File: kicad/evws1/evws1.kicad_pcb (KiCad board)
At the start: 4 copper layers, 112 x 144 mm, 216 parts, among them J1 Screw_Terminal_01x03, J10 Screw_Terminal_01x04, J11 USB 2.0 Mini, J12 USB 2.0 Mini, J13 atmega-isp-6, J14 header, J15 Jumper, J16 header, J17 header, J18 header, J19 header, J2 Screw_Terminal_01x02, J20 header, J3 HB9500-2P, J4 HB9500-3P, J5 Screw_Terminal_01x04, J6 Screw_Terminal_01x03, J7 Screw_Terminal_01x02, J8 HB9500-2P, J9 HB9500-3P, K1 G3MB-202P, K2 G3MB-202P, M1 HLK-PM01, M2 dc-dc-buck-converter-5v-to-3.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, M3 dc-dc-converter-5v-to-p12v-m1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, M5 rpi-ev-plc-adapter-v1.0, Q1 AO3401, Q2 AO3401, Q3 AO3400, Q4 AO3400, Q5 AO3401, Q6 AO3401, Q7 AO3400, SW1 SW_SS13F06-G5, SW2 SW_SS13F06-G5, SW3 SW_Push, SW4 dip-switch-4x2pos-smd-1.27mm, SW5 SS-12D00G3, SW6 SS-12D00G3, SW7 SS-12D00G3, T1 ZMPT101B, T2 ZMPT101B, U1 atmega324p-20au, U10 max485esa, U11 PC817C, U12 LM258, U2 ACS712-30, U3 ACS712-30, U4 PCF8591, U5 ch340g, U6 ch340g, U7 DS1307ZN, U8 24LC512, U9 PCF8574, Y1 20MHz, Y2 12MHz, Y3 12MHz, Y4 32768kHz

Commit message: ...
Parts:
- added C40: 100n, Project:c-1206-hand-soldering, F.Cu at (249.4, -32.6)
- added C41: 10n, Project:c-1206-hand-soldering, F.Cu at (236.9, -34.9)
- added C42: 10n, Project:c-1206-hand-soldering, F.Cu at (236.9, -32.6)
- added C43: 10n, Project:c-1206-hand-soldering, F.Cu at (236.9, -30.4)
- added C44: 10n, Project:c-1206-hand-soldering, F.Cu at (243.2, -34.9)
- added C45: 1n, Project:c-1206-hand-soldering, F.Cu at (243.2, -32.6)
- added C46: 1n, Project:c-1206-hand-soldering, F.Cu at (249.4, -34.9)
- added C47: 1n, Project:c-1206-hand-soldering, F.Cu at (272.7, -40.5)
- added C48: 1n, Project:c-1206-hand-soldering, F.Cu at (279.0, -45.0)
- added C49: 1u, Project:c-1206-hand-soldering, F.Cu at (272.7, -42.8)
- added C50: 1u, Project:c-1206-hand-soldering, F.Cu at (272.7, -45.0)
- added C51: 100n, Project:c-1206-hand-soldering, F.Cu at (236.9, -23.6)
- added R76: 10R, Project:r-0805-hand-soldering, F.Cu at (263.5, 145.1)
- added R77: 10R, Project:r-0805-hand-soldering, F.Cu at (263.5, 146.9)
- added R78: 150R, Project:r-0805-hand-soldering, F.Cu at (268.0, 145.1)
- added R79: 330R, Project:r-0805-hand-soldering, F.Cu at (263.5, 148.8)
- added R80: 330R, Project:r-0805-hand-soldering, F.Cu at (268.0, 146.9)
- added R81: 820R, Project:r-0805-hand-soldering, F.Cu at (242.3, -28.7)
- added R82: 820R, Project:r-0805-hand-soldering, F.Cu at (246.7, -30.6)
- added R83: 1K2, Project:r-0805-hand-soldering, F.Cu at (254.8, -35.1)
- added R84: 1K2, Project:r-0805-hand-soldering, F.Cu at (259.2, -33.2)
- added R85: 18K, Project:r-0805-hand-soldering, F.Cu at (242.3, -30.6)
- added R86: 0R, Project:r-0805-hand-soldering, F.Cu at (246.7, -28.7)
- added R87: 18K, Project:r-0805-hand-soldering, F.Cu at (259.2, -35.1)
- added R88: 0R, Project:r-0805-hand-soldering, F.Cu at (251.2, -30.6)
- added R89: 15K, Project:r-0805-hand-soldering, F.Cu at (251.2, -28.7)
- added R90: 15K, Project:r-0805-hand-soldering, F.Cu at (254.8, -33.2)
- added R91: 22K, Project:r-0805-hand-soldering, F.Cu at (278.1, -43.0)
- added R92: 22K, Project:r-0805-hand-soldering, F.Cu at (278.1, -41.1)
- added R93: 560R, Project:r-0805-hand-soldering, F.Cu at (278.1, -39.3)
- added RV2: 100R, Project:trimmer-tht-3296, F.Cu at (262.7, -38.5)
- added RV3: 100R, Project:trimmer-tht-3296, F.Cu at (257.4, -38.5)
- added RV4: 1K, Project:trimmer-tht-3296, F.Cu at (252.2, -38.5)
- added RV5: 1K, Project:trimmer-tht-3296, F.Cu at (246.9, -38.5)
- added RV6: 1K, Project:trimmer-tht-3296, F.Cu at (241.7, -38.5)
- added RV7: 1K, Project:trimmer-tht-3296, F.Cu at (236.4, -38.5)
- added U13: LM224, Project:soic-16_hand-soldering, F.Cu at (288.3, -12.9)
- R18: value 22K -> 10K
- R59, R60: value 22k -> 100R
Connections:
- net VREF-2V5 renamed /Measurement/VREF+2V5
- C27 pad 2: +3V3 -> +12V
- C28 pad 1: /Microcontroller/AD-VC2 -> Net-(C28-Pad1)
- D11 pad 1: /Microcontroller/AD-VC2 -> Net-(C28-Pad1)
- D16 pad 1: (no net) -> /MODBUS-B
- D16 pad 2: (no net) -> /MODBUS-A
- D16 pad 3: (no net) -> GND
- D9 pad 3: Net-(D9-Pad3) -> (no net)
- J17 pad 1: (no net) -> GND
- J17 pad 2: (no net) -> Net-(J17-Pad2)
- J17 pad 3: (no net) -> Net-(J17-Pad3)
- J18 pad 1: (no net) -> /MODBUS-A
- J18 pad 2: (no net) -> Net-(J18-Pad2)
- J19 pad 1: (no net) -> /MODBUS-B
- J19 pad 2: (no net) -> Net-(J19-Pad2)
- J20 pad 1: (no net) -> Net-(J20-Pad1)
- J20 pad 2: (no net) -> /MODBUS-A
- J6 pad 1: (no net) -> /MODBUS-A
- J6 pad 2: (no net) -> /MODBUS-B
- R53 pad 2: Net-(D9-Pad3) -> Net-(R53-Pad2)
- R54 pad 1: Net-(D9-Pad3) -> Net-(R53-Pad2)
- R59 pad 1: Net-(R59-Pad1) -> Net-(C41-Pad1)
- R59 pad 2: GND -> /Measurement/V1P
- R6 pad 1: V1P -> /Measurement/V1P
- R6 pad 2: V1N -> GND
- R60 pad 1: Net-(R60-Pad1) -> Net-(C42-Pad1)
- R60 pad 2: GND -> /Measurement/V2P
- R61 pad 1: /Microcontroller/AD-VC2 -> Net-(C28-Pad1)
- R7 pad 1: V2P -> /Measurement/V2P
- R7 pad 2: V2N -> GND
- T1 pad 3: V1P -> /Measurement/V1P
- T1 pad 4: V1N -> GND
- T2 pad 3: V2N -> GND
- T2 pad 4: V2P -> /Measurement/V2P
- U1 pad 34: (no net) -> /Measurement/AD-I2
- U1 pad 35: (no net) -> /Measurement/AD-V2
- U1 pad 36: (no net) -> /Measurement/AD-I1
- U1 pad 37: (no net) -> /Measurement/AD-V1
- U10 pad 6: (no net) -> Net-(J17-Pad2)
- U10 pad 7: (no net) -> Net-(J17-Pad3)
- U12 pad 2: /Microcontroller/AD-VC2 -> Net-(C28-Pad1)
- U12 pad 3: Net-(D9-Pad3) -> Net-(R53-Pad2)
- U12 pad 4: GND -> -12V
- U12 pad 5: Net-(R59-Pad1) -> GND
- U12 pad 6: Net-(R60-Pad1) -> Net-(R91-Pad1)
- U12 pad 7: (no net) -> /Measurement/VREF-2V5
- U12 pad 8: +3V3 -> +12V
- U2 pad 7: (no net) -> /Measurement/I1
- U3 pad 7: (no net) -> /Measurement/I2

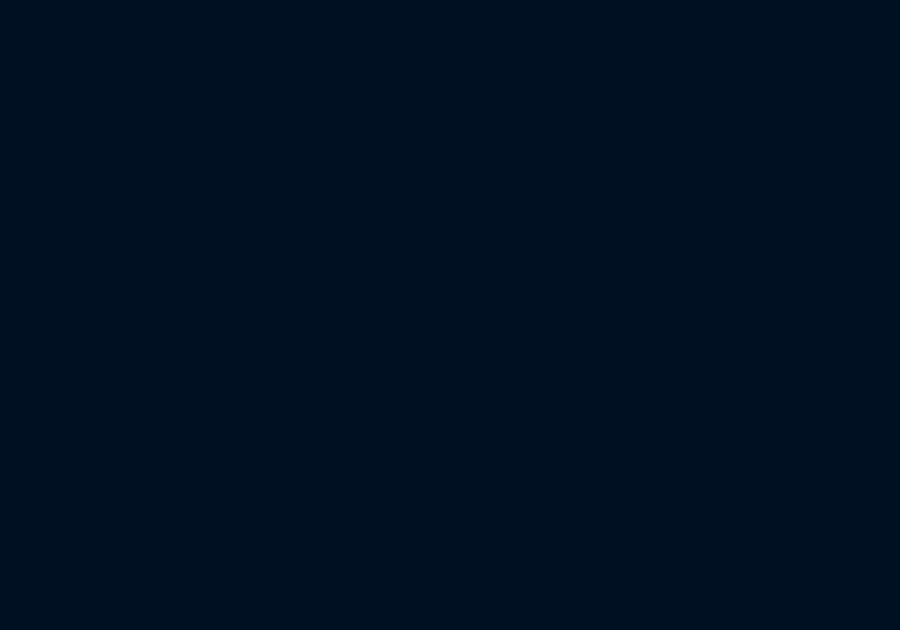
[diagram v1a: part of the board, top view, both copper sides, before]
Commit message: Schematic completed, no DRC errors left
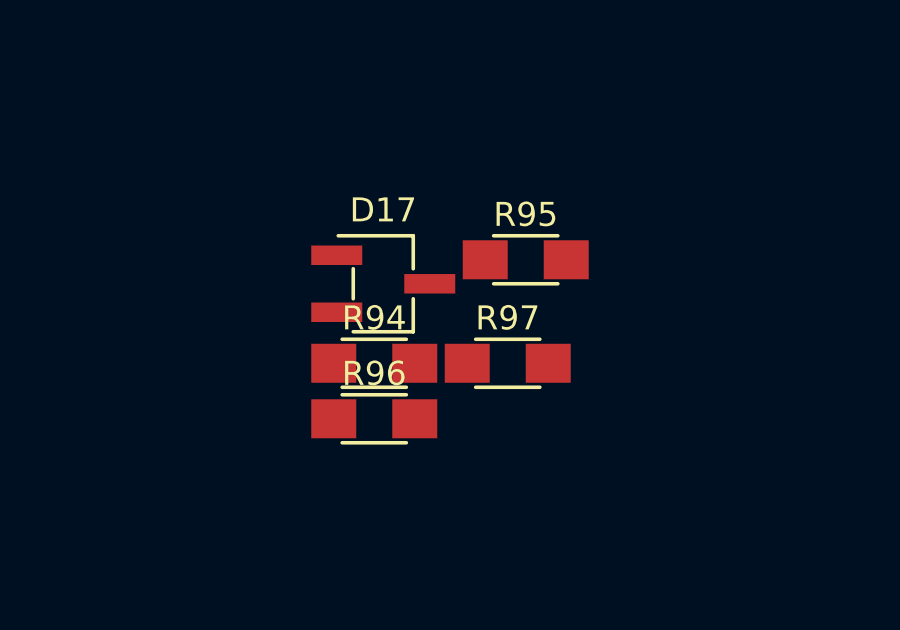
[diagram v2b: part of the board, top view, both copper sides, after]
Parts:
- added D17: BAT54S, Project:sot-23_hand-soldering, F.Cu at (196.8, -15.3)
- added R94: 100R, Project:r-0805-hand-soldering, F.Cu at (196.5, -12.7)
- added R95: 100R, Project:r-0805-hand-soldering, F.Cu at (201.6, -16.1)
- added R96: 47K, Project:r-0805-hand-soldering, F.Cu at (196.5, -10.8)
- added R97: 47K, Project:r-0805-hand-soldering, F.Cu at (201.0, -12.7)
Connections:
- net Net-(J5-Pad1) renamed /EV1TP
- D9 pad 2: +3V3 -> +5V
- D9 pad 3: (no net) -> /EV1X
- J10 pad 1: Net-(J10-Pad1) -> /EV2TP
- J10 pad 3: (no net) -> GND
- JP1 pad 2: Net-(J10-Pad1) -> (no net)
- R76 pad 1: (no net) -> /MODBUS-A
- SW4 pad 5: (no net) -> /EV1X
- SW4 pad 7: (no net) -> /EV2X
- TP1 pad 1: Net-(J10-Pad1) -> /EV2TP
- U9 pad 4: (no net) -> /Microcontroller/K2-IS-ON
- U9 pad 5: /Microcontroller/K2-IS-ON -> /Microcontroller/K1-IS-ON
- U9 pad 6: /Microcontroller/K1-IS-ON -> /EV1X
- U9 pad 7: (no net) -> /EV2X

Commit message: schematic finished
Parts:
- added D18: BAT54S, Project:sot-23_hand-soldering, F.Cu at (402.9, 27.9)
- added D19: BAT54S, Project:sot-23_hand-soldering, F.Cu at (402.9, 31.4)
- added D20: LED, LEDs:LED_0805_HandSoldering, F.Cu at (129.4, -16.4)
- added J21: header, Project:idc-header-1x03-p2.54mm-vertical, F.Cu at (395.9, 27.7)
- added J22: header, Project:idc-header-1x03-p2.54mm-vertical, F.Cu at (398.9, 27.7)
- added J23: header, Project:idc-header-1x02-p2.54mm-vertical, F.Cu at (128.5, -21.4)
- added J24: header, Project:idc-header-1x03-p2.54mm-vertical, F.Cu at (320.7, 48.1)
- added J25: header, Project:idc-header-1x04-p2.54mm-vertical, F.Cu at (167.1, 88.2)
- added R100: 47K, Project:r-0805-hand-soldering, F.Cu at (132.2, -20.2)
- added R101: 47K, Project:r-0805-hand-soldering, F.Cu at (132.2, -18.3)
- added R102: 220R, Project:r-0805-hand-soldering, F.Cu at (134.0, -16.5)
- added R103: 1K, Project:r-0805-hand-soldering, F.Cu at (136.7, -20.2)
- added R104: 270R, Project:r-0805-hand-soldering, F.Cu at (321.5, 55.6)
- added R105: 560R, Project:r-0805-hand-soldering, F.Cu at (324.4, 47.5)
- added R98: 47K, Project:r-0805-hand-soldering, F.Cu at (132.2, -22.0)
- added R99: 47K, Project:r-0805-hand-soldering, F.Cu at (136.7, -22.0)
- added SW8: dip-switch-4x2pos-smd-1.27mm, Project:dip-switch-4x2pos-smd-1.27mm, F.Cu at (315.6, 51.5)
- added TP7: TestPoint, Measurement_Points:Measurement_Point_Round-TH_Small, F.Cu at (115.2, 59.7)
- added TP8: TestPoint, Wire_Pads:SolderWirePad_single_0-8mmDrill, F.Cu at (79.8, 22.4)
- added TP9: TestPoint, Wire_Pads:SolderWirePad_single_0-8mmDrill, F.Cu at (165.8, 43.7)
- C23: footprint Capacitors_THT:C_Disc_D3.8mm_W2.6mm_P2.50mm -> Project:capacitor-ceramic-tht-2200pf-1000v
- R1: value 220K -> 0R; footprint Project:r-0805-hand-soldering -> Project:r-1206-hand-soldering
- R27, R28: value 1K -> 10K
- R6, R7: value 100R -> 1K
- R62, R72: value 100R -> 180R
- R83, R84: value 1K2 -> 3K3
- R85, R87: value 18K -> 15K
- R86, R88: value 0R -> 4K7
- R89, R90: value 15K -> 10K
- R94, R95: value 100R -> 330R
- TP1, TP4: footprint Measurement_Points:Measurement_Point_Round-TH_Big -> Measurement_Points:Measurement_Point_Round-TH_Small
- moved C23 8.82 mm to (266.2, 26.3)
- moved C1 1.98 mm to (53.2, 98.4)
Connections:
- C43 pad 2: /Measurement/AD-V1 -> Net-(C43-Pad2)
- C44 pad 2: /Measurement/AD-V2 -> Net-(C44-Pad2)
- D7 pad 3: /Microcontroller/MISO -> /Microcontroller/Converter-And-Cp/MISO-IN
- D8 pad 3: /Microcontroller/IRQ-MODEM -> /Microcontroller/Converter-And-Cp/IRQ-IN
- JP2 pad 1: /Microcontroller/CONNECTED -> Net-(JP2-Pad1)
- JP3 pad 1: /Microcontroller/CONNECTED -> Net-(JP2-Pad1)
- R6 pad 1: /Measurement/V1P -> /Measurement/AD-V1
- R6 pad 2: GND -> Net-(C43-Pad2)
- R7 pad 1: /Measurement/V2P -> /Measurement/AD-V2
- R7 pad 2: GND -> Net-(C44-Pad2)
- R89 pad 1: /Measurement/AD-V1 -> Net-(C43-Pad2)
- R90 pad 1: /Measurement/AD-V2 -> Net-(C44-Pad2)
- SW5 pad 1: Net-(Q3-Pad1) -> Net-(R22-Pad2)
- SW5 pad 2: Net-(R22-Pad2) -> Net-(Q3-Pad1)
- SW5 pad 3: (no net) -> Net-(R102-Pad2)
- T1 pad 2: /N-K1 -> /N-EV1
- T1 pad 3: /Measurement/V1P -> GND
- T1 pad 4: GND -> /Measurement/V1P
- U1 pad 21: /Microcontroller/IRQ-MODEM -> /Microcontroller/IRQ-PORTEXP
- U1 pad 30: /Microcontroller/CONNECTED -> /Microcontroller/DEBUG
- U1 pad 31: /Microcontroller/IRQ-PORTEXP -> /Microcontroller/LCD-RW
- U1 pad 40: /Microcontroller/LCD-RS -> Net-(J24-Pad2)
- U1 pad 41: /Microcontroller/LCD-RW -> Net-(J24-Pad3)
- U1 pad 42: /Microcontroller/~K1-ON -> /Microcontroller/LCD-RS
- U1 pad 43: /Microcontroller/~K2-ON -> /Microcontroller/IRQ-MODEM
- U13 pad 14: /Measurement/AD-V2 -> Net-(C44-Pad2)
- U13 pad 7: /Measurement/AD-V1 -> Net-(C43-Pad2)
- U9 pad 10: (no net) -> /EV2X
- U9 pad 4: /Microcontroller/K2-IS-ON -> /Microcontroller/PEXP-P0
- U9 pad 5: /Microcontroller/K1-IS-ON -> /Microcontroller/PEXP-P1
- U9 pad 6: /EV1X -> /Microcontroller/K2-IS-ON
- U9 pad 7: /EV2X -> /Microcontroller/K1-IS-ON
- U9 pad 9: (no net) -> /EV1X

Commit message: ...
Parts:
- removed JP1: SolderJumper_3_Open, Pin_Headers:Pin_Header_Straight_1x03_Pitch2.54mm
- added C52: 100n, Project:c-1206-hand-soldering, B.Cu at (64.6, 103.5)
- added C53: 100n, Project:c-1206-hand-soldering, B.Cu at (117.9, 110.5)
- added C54: 100n, Project:c-1206-hand-soldering, B.Cu at (67.0, 111.3)
- added J26: header, Project:idc-header-1x02-p2.54mm-vertical, F.Cu at (92.7, 42.6)
- added U14: LM258, Project:soic-8_hand-soldering, B.Cu at (65.8, 107.4)
- BT1: footprint Project:knob-battery-holder-horizontal-tht -> Project:knob-battery-holder-vertical-tht
- C10, C11, C12, C13, C14, C15, C16, C17, C19, C20, C21, C22, C24, C25, C26, C27, C28, C37, C39, C40, C41, C42, C43, C44, C45, C46, C47, C48, C49, C50, C51, C6, C7, C8, C9, D1, D10, D11, D12, D13, D14, D15, D16, D17, D18, D19, D2, D5, D6, D7, D8, D9, L1, Q3, Q4, Q5, Q6, Q7, R1, R100, R101, R102, R103, R104, R105, R18, R19, R20, R21, R22, R23, R24, R25, R26, R27, R28, R29, R30, R31, R32, R33, R34, R35, R36, R37, R38, R39, R40, R41, R42, R43, R44, R45, R46, R47, R48, R49, R50, R51, R52, R53, R54, R55, R56, R57, R58, R59, R60, R61, R62, R63, R64, R65, R66, R67, R68, R69, R70, R71, R72, R73, R74, R75, R76, R77, R78, R79, R80, R81, R82, R83, R84, R85, R86, R87, R88, R89, R90, R91, R92, R93, R94, R95, R96, R97, R98, R99, U10, U11, U12, U4, U8, U9: moved to B.Cu
- C23: footprint Project:capacitor-ceramic-tht-2200pf-1000v -> Project:c-1206-hand-soldering; moved to B.Cu
- RV3: value 100R -> 1K
- RV4: value 1K -> 100R
- SW3: footprint Buttons_Switches_SMD:SW_SPST_FSMSM -> Project:push-button-smd-4.5x4.5mm-black
- U13: value LM224 -> LM258; footprint Project:soic-16_hand-soldering -> Project:soic-8_hand-soldering; moved to B.Cu
- U5, Y2: moved to F.Cu
- moved J22 349.7 mm to (58.8, 109.0), turned to 180 degrees
- moved D19 339.2 mm to (71.2, 102.4)
- moved D18 289.2 mm to (125.8, 111.0), turned to 90 degrees
- moved J21 278.9 mm to (129.3, 109.7), turned to 180 degrees
- moved J24 269.9 mm to (67.2, 140.6), turned to 90 degrees
- moved R105 266.1 mm to (62.1, 92.2), turned to 90 degrees
- moved R104 264.0 mm to (60.0, 92.0), turned to 270 degrees
- moved R87 250.5 mm to (64.0, 121.8)
- moved D9 243.5 mm to (27.2, 90.0)
- moved R88 240.0 mm to (64.0, 119.7), turned to 180 degrees
- moved RV4 238.9 mm to (77.2, 124.2)
- moved C46 238.6 mm to (68.3, 120.5), turned to 270 degrees
- moved RV7 232.1 mm to (70.9, 124.2)
- moved R84 231.7 mm to (76.9, 109.8)
- moved RV5 231.3 mm to (82.5, 124.2)
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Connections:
- net Net-(F1-Pad2) renamed /Microcontroller/UARTs/Modbus/UART0-5V
- net Net-(F2-Pad2) renamed /Microcontroller/UARTs/Modbus/UART1-5V
- net Net-(J11-Pad2) renamed /Microcontroller/UARTs/Modbus/USB0-D-
- net Net-(J11-Pad3) renamed /Microcontroller/UARTs/Modbus/USB0-D+
- net Net-(J12-Pad2) renamed /Microcontroller/UARTs/Modbus/USB1-D-
- net Net-(J12-Pad3) renamed /Microcontroller/UARTs/Modbus/USB1-D+
- D16 pad 1: /MODBUS-B -> /MODBUS-A
- D16 pad 2: /MODBUS-A -> /MODBUS-B
- J5 pad 1: /EV1TP -> /CP1
- J5 pad 2: /~EV1ON -> GND
- J5 pad 3: GND -> /~EV1ON
- J5 pad 4: /CP1 -> /EV1TP
- J6 pad 1: /MODBUS-A -> GND
- J6 pad 3: GND -> /MODBUS-A
- M1 pad 3: 230V-N -> 230V-L
- M1 pad 4: 230V-L -> 230V-N
- Q5 pad 2: +3V3 -> +5V
- R47 pad 2: +3V3 -> +5V
- R76 pad 2: Net-(J17-Pad2) -> Net-(J17-Pad3)
- R77 pad 2: Net-(J17-Pad3) -> Net-(J17-Pad2)
- RV3 pad 1: Net-(C42-Pad2) -> Net-(R85-Pad2)
- RV3 pad 2: Net-(C42-Pad2) -> Net-(R85-Pad2)
- RV3 pad 3: Net-(R82-Pad1) -> /Measurement/VREF-2V5
- RV4 pad 1: Net-(R85-Pad2) -> Net-(C42-Pad2)
- RV4 pad 2: Net-(R85-Pad2) -> Net-(C42-Pad2)
- RV4 pad 3: /Measurement/VREF-2V5 -> Net-(R82-Pad1)
- TP7 pad 1: +BATT -> /Microcontroller/AOUT
- U10 pad 6: Net-(J17-Pad2) -> Net-(J17-Pad3)
- U10 pad 7: Net-(J17-Pad3) -> Net-(J17-Pad2)
- U13 pad 8: Net-(C42-Pad2) -> -12V
- U4 pad 15: (no net) -> /Microcontroller/AOUT

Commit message: ...
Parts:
- M1: footprint Project:HLK-PM01 -> Project:HLK-PM01-5M05
- R10, R100, R101, R102, R103, R104, R105, R11, R12, R13, R14, R15, R16, R17, R18, R19, R2, R20, R21, R22, R23, R24, R25, R26, R27, R28, R29, R3, R30, R31, R32, R33, R34, R35, R36, R37, R38, R39, R4, R40, R42, R43, R44, R45, R46, R47, R48, R49, R5, R50, R51, R52, R53, R54, R55, R56, R57, R58, R59, R6, R60, R61, R62, R63, R64, R65, R66, R67, R68, R69, R7, R70, R71, R72, R73, R74, R75, R76, R77, R78, R79, R8, R80, R81, R82, R83, R84, R85, R86, R87, R88, R89, R9, R90, R91, R92, R93, R94, R95, R96, R97, R98, R99: footprint Project:r-0805-hand-soldering -> Project:r-1206-hand-soldering
- moved C47 144.9 mm to (8.05, 87.3)
- moved C48 144.9 mm to (14.8, 107.8)
- moved C49 144.9 mm to (7.85, 107.8)
- moved C50 144.9 mm to (1.25, 87.4)
- moved Q4 144.9 mm to (15.4, 91.2)
- moved Q5 144.9 mm to (14.9, 104.1)
- moved Q6 144.9 mm to (14.3, 84.2)
- moved Q7 144.9 mm to (22.2, 108.2)
- moved R46 144.9 mm to (14.1, 87.3)
- moved R47 144.9 mm to (19.7, 103.7)
- moved R48 144.9 mm to (9.75, 104.3)
- moved R49 144.9 mm to (8.15, 85.0)
- moved R50 144.9 mm to (18.6, 112.0)
- moved R51 144.9 mm to (20.4, 84.1)
- moved R52 144.9 mm to (27.6, 108.2)
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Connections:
- J18 pad 1: /MODBUS-A -> Net-(J18-Pad1)
- J18 pad 2: Net-(J18-Pad2) -> /MODBUS-A
- R78 pad 1: Net-(J18-Pad2) -> Net-(J18-Pad1)

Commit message: ...
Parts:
- removed C27: 100n, Project:c-1206-hand-soldering
- removed the R90 at (75.3, 106.5)
- removed the R93 at (199.8, 76.2)
- removed the TP2 at (101.5, 129.6)
- removed U14: LM258, Project:soic-8_hand-soldering
- added R106: 0R, Project:r-1206-hand-soldering, B.Cu at (124.4, 82.8)
- added R4: 10K, Project:r-1206-hand-soldering, F.Cu at (98.8, 114.7)
- added R5: 560R, Project:r-1206-hand-soldering, F.Cu at (92.7, 113.9)
- C10, C11, C12, C13, C16, C17, C28, C41, C42, C43, C44, C45, C46, C47, C48, C49, C50, C51, C6, C7, C8, C9, D11, D18, D19, D2, D5, L1, Q4, Q5, Q6, Q7, R18, R19, R46, R47, R48, R49, R50, R51, R52, R53, R54, R6, R61, R7, R81, R82, R83, R84, R85, R86, R87, R88, R89, R91, R92, U12: moved to F.Cu
- J21, J22: footprint Project:idc-header-1x03-p2.54mm-vertical -> Project:idc-header-1x04-p2.54mm-vertical
- M2, M3: moved to B.Cu
- TP3: footprint Wire_Pads:SolderWirePad_single_0-8mmDrill -> Measurement_Points:Measurement_Point_Round-TH_Small
- U13: value LM258 -> LM224; footprint Project:soic-8_hand-soldering -> Project:soic-14_hand-soldering; moved to F.Cu
- moved R33 298.5 mm to (-9.33, 132.1)
- moved R34 292.9 mm to (-2.65, 132.1)
- moved R32 263.3 mm to (14.2, 79.0), turned to 0 degrees
- moved U9 252.2 mm to (17.7, 87.7), turned to 90 degrees
- moved C22 247.1 mm to (24.4, 84.6), turned to 90 degrees
- moved R31 244.5 mm to (17.3, 97.2), turned to 180 degrees
- moved R24 240.8 mm to (27.6, 148.6)
- moved R39 240.8 mm to (32.1, 159.9)
- moved R25 240.8 mm to (27.4, 154.7)
- moved R35 240.8 mm to (27.3, 159.9)
- moved R36 240.8 mm to (27.2, 165.3)
- moved R40 240.8 mm to (31.9, 165.3)
- moved R37 240.8 mm to (32.9, 148.5)
- moved R38 240.8 mm to (32.4, 154.7)
- moved R18 144.4 mm to (78.0, 123.5), turned to 180 degrees
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- renumbered R4 to R90, R5 to R93, TP4 to TP2
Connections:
- C45 pad 2: /Measurement/AD-I1 -> /AD-I1
- C46 pad 2: /Measurement/AD-I2 -> /AD-I2
- D10 pad 2: /CP2 -> /CP1
- D18 pad 3: /Measurement/AD-V1 -> /AD-V1
- D19 pad 3: /Measurement/AD-V2 -> /AD-V2
- J11 pad 4: (no net) -> Net-(J11-Pad4)
- J12 pad 4: (no net) -> Net-(J12-Pad4)
- J13 pad 3: /Microcontroller/MISO -> /Microcontroller/SCK
- J21 pad 2: /Measurement/AD-V1 -> /CP1
- J21 pad 3: /Measurement/AD-I1 -> /AD-I1
- J22 pad 2: /Measurement/AD-V2 -> /CP2
- J22 pad 3: /Measurement/AD-I2 -> /AD-I2
- J25 pad 2: /Microcontroller/SDA -> Net-(J25-Pad2)
- J25 pad 3: /Microcontroller/SCL -> /Microcontroller/SDA
- J25 pad 4: /Microcontroller/IRQ-PORTEXP -> /Microcontroller/SCL
- M5 pad 10: (no net) -> Net-(M5-Pad10)
- M5 pad 11: (no net) -> Net-(M5-Pad11)
- M5 pad 12: (no net) -> Net-(M5-Pad12)
- M5 pad 16: (no net) -> Net-(M5-Pad16)
- M5 pad 27: (no net) -> Net-(M5-Pad27)
- M5 pad 28: (no net) -> Net-(M5-Pad28)
- M5 pad 29: (no net) -> Net-(M5-Pad29)
- M5 pad 31: (no net) -> Net-(M5-Pad31)
- M5 pad 33: (no net) -> Net-(M5-Pad33)
- M5 pad 35: (no net) -> Net-(M5-Pad35)
- M5 pad 36: (no net) -> Net-(M5-Pad36)
- M5 pad 37: (no net) -> Net-(M5-Pad37)
- M5 pad 38: (no net) -> Net-(M5-Pad38)
- M5 pad 40: (no net) -> Net-(M5-Pad40)
- M5 pad 42: /Microcontroller/AD-VC1 -> /Microcontroller/AD-VC2
- M5 pad 54: (no net) -> Net-(M5-Pad54)
- M5 pad 56: /CP1 -> /CP2
- M5 pad 57: (no net) -> Net-(M5-Pad57)
- M5 pad 58: (no net) -> Net-(M5-Pad58)
- M5 pad 59: (no net) -> Net-(M5-Pad59)
- M5 pad 7: (no net) -> Net-(M5-Pad7)
- M5 pad 8: (no net) -> Net-(M5-Pad8)
- R51 pad 2: /CP2 -> /CP1
- R52 pad 1: /CP2 -> /CP1
- R53 pad 1: /CP2 -> /CP1
- R6 pad 1: /Measurement/AD-V1 -> /AD-V1
- R7 pad 1: /Measurement/AD-V2 -> /AD-V2
- RV6 pad 2: /Measurement/AD-I1 -> /AD-I1
- RV7 pad 2: /Measurement/AD-I2 -> /AD-I2
- SW1 pad 1: (no net) -> Net-(SW1-Pad1)
- SW2 pad 1: (no net) -> Net-(SW2-Pad1)
- SW4 pad 1: /Microcontroller/~RESET1 -> Net-(C10-Pad2)
- SW4 pad 2: Net-(C7-Pad2) -> /EV2X
- SW4 pad 3: /Microcontroller/~RESET2 -> Net-(C9-Pad2)
- SW4 pad 4: Net-(C8-Pad2) -> /EV1X
- SW4 pad 5: /EV1X -> Net-(C7-Pad2)
- SW4 pad 6: Net-(C9-Pad2) -> /Microcontroller/~RESET1
- SW4 pad 7: /EV2X -> Net-(C8-Pad2)
- SW4 pad 8: Net-(C10-Pad2) -> /Microcontroller/~RESET2
- SW6 pad 3: (no net) -> Net-(SW6-Pad3)
- SW7 pad 3: (no net) -> Net-(SW7-Pad3)
- SW8 pad 1: /Microcontroller/PEXP-P0 -> /Microcontroller/~K2-ON
- SW8 pad 2: /Microcontroller/~K1-ON -> Net-(J24-Pad3)
- SW8 pad 3: Net-(J24-Pad2) -> /Microcontroller/~K2-ON
- SW8 pad 4: /Microcontroller/~K1-ON -> /Microcontroller/PEXP-P1
- SW8 pad 5: Net-(J24-Pad3) -> /Microcontroller/~K1-ON
- SW8 pad 6: /Microcontroller/~K2-ON -> /Microcontroller/PEXP-P0
- SW8 pad 7: /Microcontroller/PEXP-P1 -> /Microcontroller/~K1-ON
- SW8 pad 8: /Microcontroller/~K2-ON -> Net-(J24-Pad2)
- TP3 pad 1: Net-(M5-Pad13) -> /Microcontroller/IRQ-PORTEXP
- U1 pad 32: /Microcontroller/AD-VC1 -> /AD-I2
- U1 pad 33: /Microcontroller/AD-VC2 -> /AD-I1
- U1 pad 34: /Measurement/AD-I2 -> /AD-V2
- U1 pad 35: /Measurement/AD-V2 -> /Microcontroller/AD-VC1
- U1 pad 36: /Measurement/AD-I1 -> /Microcontroller/AD-VC2
- U1 pad 37: /Measurement/AD-V1 -> /AD-V1
- U13 pad 1: Net-(C41-Pad2) -> Net-(C44-Pad2)
- U13 pad 2: Net-(C41-Pad1) -> Net-(C44-Pad1)
- U13 pad 6: Net-(C43-Pad1) -> Net-(C42-Pad1)
- U13 pad 7: Net-(C43-Pad2) -> Net-(C42-Pad2)
- U13 pad 8: -12V -> Net-(C41-Pad2)
- U4 pad 11: (no net) -> Net-(U4-Pad11)
- U5 pad 10: (no net) -> Net-(U5-Pad10)
- U5 pad 11: (no net) -> Net-(U5-Pad11)
- U5 pad 12: (no net) -> Net-(U5-Pad12)
- U5 pad 14: (no net) -> Net-(U5-Pad14)
- U5 pad 15: (no net) -> Net-(U5-Pad15)
- U5 pad 9: (no net) -> Net-(U5-Pad9)
- U6 pad 10: (no net) -> Net-(U6-Pad10)
- U6 pad 11: (no net) -> Net-(U6-Pad11)
- U6 pad 12: (no net) -> Net-(U6-Pad12)
- U6 pad 14: (no net) -> Net-(U6-Pad14)
- U6 pad 15: (no net) -> Net-(U6-Pad15)
- U6 pad 9: (no net) -> Net-(U6-Pad9)
- U7 pad 7: (no net) -> Net-(U7-Pad7)
